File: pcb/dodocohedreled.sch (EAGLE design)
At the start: 11 parts

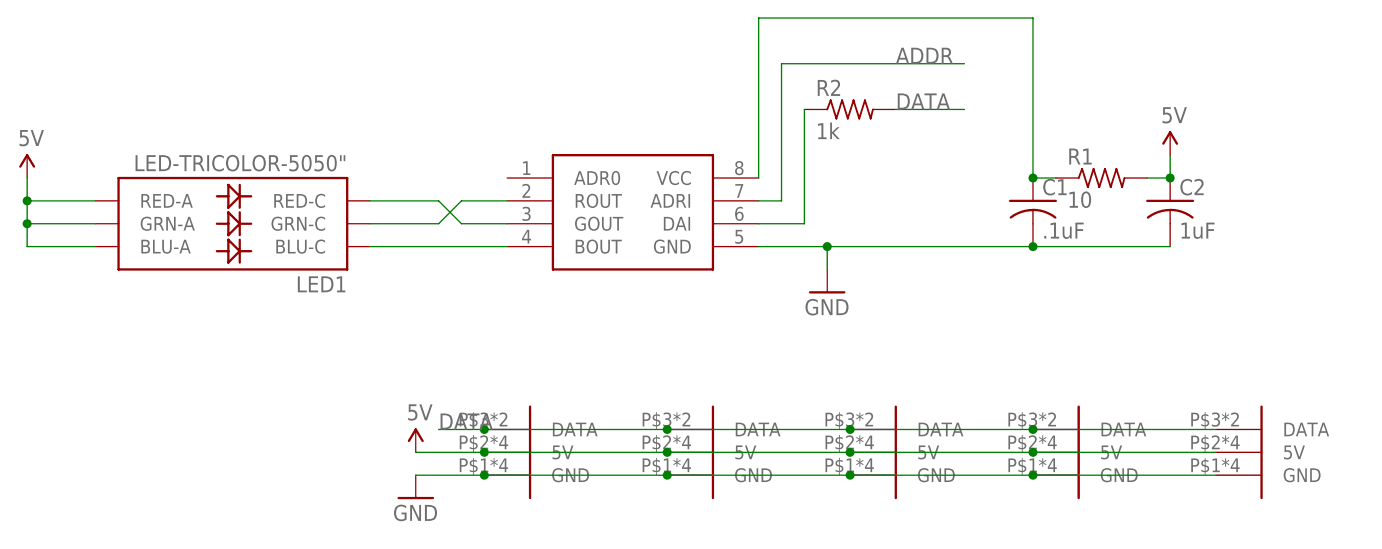
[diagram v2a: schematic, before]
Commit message: Switch to WS2822S module, bump to RevD.
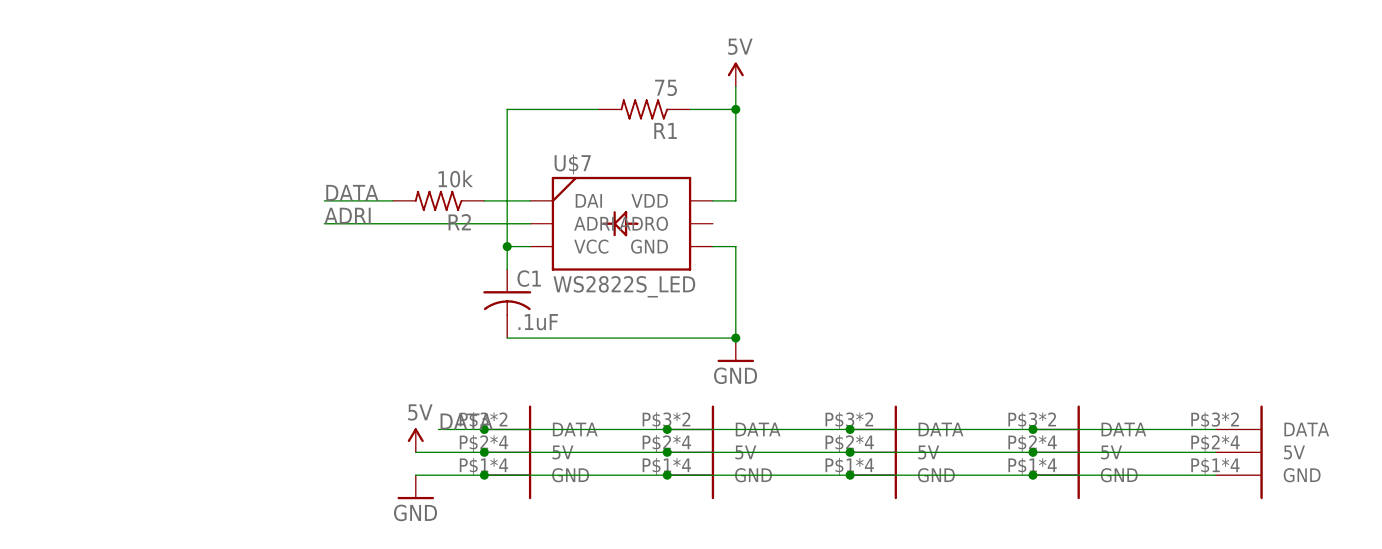
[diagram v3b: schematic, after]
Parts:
- removed C2: 1uF, adafruit:C-USC0603
- removed LED1: LED-TRICOLOR-5050", blinkinlabs:LED-TRICOLOR-5050"
- removed U$1: WS2821A, dodocohedreled:WS2821A
- added U$7: WS2822S_LED, blinkinlabs:WS2822S_LED
- R1: value 10 -> 75
- R2: value 1k -> 10k
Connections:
- removed net ADDR: U$1.ADRI
- removed net N$10: R2.1, U$1.DAI
- removed net N$3: LED1.RED-C, U$1.GOUT
- removed net N$6: C1.1, R1.1, U$1.VCC
- new net ADRI: U$7.ADRI
- net 5V: now also R1.1, U$7.VDD; no longer C2.1, LED1.BLU-A, LED1.GRN-A, LED1.RED-A, R1.2
- net GND: now also U$7.GND; no longer C2.2, U$1.GND
- net N$1: now also C1.1, R1.2, U$7.VCC; no longer LED1.GRN-C, U$1.ROUT
- net N$2: now also R2.1, U$7.DAI; no longer LED1.BLU-C, U$1.BOUT
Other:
- moved on the sheet: C1, R1, R2
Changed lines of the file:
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@@
 <?xml version="1.0" encoding="utf-8"?>
 <!DOCTYPE eagle SYSTEM "eagle.dtd">
-<eagle version="6.5.0">
+<eagle version="7.1.0">
 <drawing>
 <settings>
@@
 </classes>
 <parts>
-<part name="LED1" library="blinkinlabs" deviceset="LED-TRICOLOR-5050" device="&quot;"/>
-<part name="SUPPLY1" library="SparkFun-Aesthetics" deviceset="5V" device=""/>
 <part name="GND1" library="SparkFun-Aesthetics" deviceset="GND" device=""/>
-<part name="U$1" library="dodocohedreled" deviceset="WS2821A" device=""/>
 <part name="C1" library="adafruit" deviceset="C-US" device="C0603" value=".1uF"/>
-<part name="C2" library="adafruit" deviceset="C-US" device="C0603" value="1uF"/>
-<part name="R1" library="adafruit" deviceset="R-US_" device="R0603" value="10"/>
-<part name="R2" library="adafruit" deviceset="R-US_" device="R0603" value="1k"/>
+<part name="R1" library="adafruit" deviceset="R-US_" device="R0603" value="75"/>
+<part name="R2" library="adafruit" deviceset="R-US_" device="R0603" value="10k"/>
 <part name="SUPPLY2" library="SparkFun-Aesthetics" deviceset="5V" device=""/>
 <part name="U$2" library="dodocohedreled" deviceset="D_EDGE" device="SLOT"/>
@@
 <part name="U$5" library="dodocohedreled" deviceset="D_EDGE" device="SLOT"/>
 <part name="U$6" library="dodocohedreled" deviceset="D_EDGE" device="SLOT"/>
+<part name="U$7" library="blinkinlabs" deviceset="WS2822S_LED" device=""/>
 </parts>
 <sheets>
@@
 </plain>
 <instances>
-<instance part="LED1" gate="G$1" x="15.24" y="81.28" rot="R180"/>
-<instance part="SUPPLY1" gate="G$1" x="-7.62" y="86.36"/>
-<instance part="GND1" gate="1" x="81.28" y="73.66"/>
-<instance part="U$1" gate="G$1" x="53.34" y="81.28"/>
-<instance part="C1" gate="G$1" x="104.14" y="83.82"/>
-<instance part="C2" gate="G$1" x="119.38" y="83.82"/>
-<instance part="R1" gate="G$1" x="111.76" y="86.36"/>
-<instance part="R2" gate="G$1" x="83.82" y="93.98"/>
-<instance part="SUPPLY2" gate="G$1" x="119.38" y="88.9"/>
+<instance part="GND1" gate="1" x="71.12" y="66.04"/>
+<instance part="C1" gate="G$1" x="45.72" y="73.66"/>
+<instance part="R1" gate="G$1" x="60.96" y="93.98" rot="R180"/>
+<instance part="R2" gate="G$1" x="38.1" y="83.82" rot="R180"/>
+<instance part="SUPPLY2" gate="G$1" x="71.12" y="96.52"/>
 <instance part="U$2" gate="G$1" x="124.46" y="58.42"/>
 <instance part="SUPPLY3" gate="G$1" x="35.56" y="55.88"/>
@@
 <instance part="U$5" gate="G$1" x="83.82" y="58.42"/>
 <instance part="U$6" gate="G$1" x="104.14" y="58.42"/>
+<instance part="U$7" gate="G$1" x="58.42" y="81.28"/>
 </instances>
 <busses>
@@
 <nets>
 <net name="5V" class="0">
-<segment>
-<pinref part="SUPPLY1" gate="G$1" pin="5V"/>
-<wire x1="-7.62" y1="86.36" x2="-7.62" y2="83.82" width="0.1524" layer="91"/>
-<pinref part="LED1" gate="G$1" pin="BLU-A"/>
-<wire x1="0" y1="78.74" x2="-7.62" y2="78.74" width="0.1524" layer="91"/>
-<wire x1="-7.62" y1="78.74" x2="-7.62" y2="81.28" width="0.1524" layer="91"/>
-<pinref part="LED1" gate="G$1" pin="GRN-A"/>
-<wire x1="0" y1="81.28" x2="-7.62" y2="81.28" width="0.1524" layer="91"/>
-<wire x1="-7.62" y1="81.28" x2="-7.62" y2="83.82" width="0.1524" layer="91"/>
-<pinref part="LED1" gate="G$1" pin="RED-A"/>
-<wire x1="-7.62" y1="83.82" x2="0" y2="83.82" width="0.1524" layer="91"/>
-<junction x="-7.62" y="81.28"/>
-<junction x="-7.62" y="83.82"/>
-</segment>
-<segment>
-<pinref part="R1" gate="G$1" pin="2"/>
-<pinref part="C2" gate="G$1" pin="1"/>
-<wire x1="116.84" y1="86.36" x2="119.38" y2="86.36" width="0.1524" layer="91"/>
-<pinref part="SUPPLY2" gate="G$1" pin="5V"/>
-<wire x1="119.38" y1="88.9" x2="119.38" y2="86.36" width="0.1524" layer="91"/>
-<junction x="119.38" y="86.36"/>
-</segment>
 <segment>
 <pinref part="U$2" gate="G$1" pin="5V"/>
@@
 <junction x="104.14" y="55.88"/>
 </segment>
-</net>
-<net name="N$2" class="0">
-<segment>
-<pinref part="LED1" gate="G$1" pin="BLU-C"/>
-<pinref part="U$1" gate="G$1" pin="BOUT"/>
-<wire x1="30.48" y1="78.74" x2="45.72" y2="78.74" width="0.1524" layer="91"/>
+<segment>
+<pinref part="U$7" gate="G$1" pin="VDD"/>
+<wire x1="68.58" y1="83.82" x2="71.12" y2="83.82" width="0.1524" layer="91"/>
+<pinref part="SUPPLY2" gate="G$1" pin="5V"/>
+<wire x1="71.12" y1="83.82" x2="71.12" y2="93.98" width="0.1524" layer="91"/>
+<pinref part="R1" gate="G$1" pin="1"/>
+<wire x1="71.12" y1="93.98" x2="71.12" y2="96.52" width="0.1524" layer="91"/>
+<wire x1="66.04" y1="93.98" x2="71.12" y2="93.98" width="0.1524" layer="91"/>
+<junction x="71.12" y="93.98"/>
 </segment>
 </net>
 <net name="GND" class="0">
 <segment>
-<pinref part="U$1" gate="G$1" pin="GND"/>
-<wire x1="73.66" y1="78.74" x2="81.28" y2="78.74" width="0.1524" layer="91"/>
+<wire x1="71.12" y1="78.74" x2="71.12" y2="68.58" width="0.1524" layer="91"/>
 <pinref part="GND1" gate="1" pin="GND"/>
-<wire x1="81.28" y1="78.74" x2="81.28" y2="76.2" width="0.1524" layer="91"/>
-<pinref part="C2" gate="G$1" pin="2"/>
 <pinref part="C1" gate="G$1" pin="2"/>
-<wire x1="119.38" y1="78.74" x2="104.14" y2="78.74" width="0.1524" layer="91"/>
-<wire x1="104.14" y1="78.74" x2="81.28" y2="78.74" width="0.1524" layer="91"/>
-<junction x="81.28" y="78.74"/>
-<junction x="104.14" y="78.74"/>
+<wire x1="45.72" y1="68.58" x2="71.12" y2="68.58" width="0.1524" layer="91"/>
+<junction x="71.12" y="68.58"/>
+<pinref part="U$7" gate="G$1" pin="GND"/>
+<wire x1="71.12" y1="78.74" x2="68.58" y2="78.74" width="0.1524" layer="91"/>
 </segment>
 <segment>
@@
 </segment>
 </net>
-<net name="N$6" class="0">
-<segment>
-<pinref part="U$1" gate="G$1" pin="VCC"/>
-<pinref part="C1" gate="G$1" pin="1"/>
-<wire x1="73.66" y1="86.36" x2="73.66" y2="104.14" width="0.1524" layer="91"/>
-<wire x1="73.66" y1="104.14" x2="104.14" y2="104.14" width="0.1524" layer="91"/>
-<wire x1="104.14" y1="104.14" x2="104.14" y2="86.36" width="0.1524" layer="91"/>
-<pinref part="R1" gate="G$1" pin="1"/>
-<wire x1="104.14" y1="86.36" x2="106.68" y2="86.36" width="0.1524" layer="91"/>
-<junction x="104.14" y="86.36"/>
-</segment>
-</net>
-<net name="ADDR" class="0">
-<segment>
-<wire x1="76.2" y1="99.06" x2="76.2" y2="83.82" width="0.1524" layer="91"/>
-<pinref part="U$1" gate="G$1" pin="ADRI"/>
-<wire x1="76.2" y1="83.82" x2="73.66" y2="83.82" width="0.1524" layer="91"/>
-<wire x1="76.2" y1="99.06" x2="96.52" y2="99.06" width="0.1524" layer="91"/>
-<label x="88.9" y="99.06" size="1.778" layer="95"/>
-</segment>
-</net>
-<net name="N$10" class="0">
-<segment>
-<pinref part="U$1" gate="G$1" pin="DAI"/>
-<pinref part="R2" gate="G$1" pin="1"/>
-<wire x1="73.66" y1="81.28" x2="78.74" y2="81.28" width="0.1524" layer="91"/>
-<wire x1="78.74" y1="81.28" x2="78.74" y2="93.98" width="0.1524" layer="91"/>
+<net name="ADRI" class="0">
+<segment>
+<wire x1="48.26" y1="81.28" x2="25.4" y2="81.28" width="0.1524" layer="91"/>
+<label x="25.4" y="81.28" size="1.778" layer="95"/>
+<pinref part="U$7" gate="G$1" pin="ADRI"/>
 </segment>
 </net>
@@
 <segment>
 <pinref part="R2" gate="G$1" pin="2"/>
-<wire x1="88.9" y1="93.98" x2="96.52" y2="93.98" width="0.1524" layer="91"/>
-<label x="88.9" y="93.98" size="1.778" layer="95"/>
+<wire x1="33.02" y1="83.82" x2="25.4" y2="83.82" width="0.1524" layer="91"/>
+<label x="25.4" y="83.82" size="1.778" layer="95"/>
 </segment>
 <segment>
@@
 <net name="N$1" class="0">
 <segment>
-<pinref part="U$1" gate="G$1" pin="ROUT"/>
-<wire x1="45.72" y1="83.82" x2="40.64" y2="83.82" width="0.1524" layer="91"/>
-<wire x1="40.64" y1="83.82" x2="38.1" y2="81.28" width="0.1524" layer="91"/>
-<pinref part="LED1" gate="G$1" pin="GRN-C"/>
-<wire x1="38.1" y1="81.28" x2="30.48" y2="81.28" width="0.1524" layer="91"/>
-</segment>
-</net>
-<net name="N$3" class="0">
-<segment>
-<pinref part="LED1" gate="G$1" pin="RED-C"/>
-<wire x1="30.48" y1="83.82" x2="38.1" y2="83.82" width="0.1524" layer="91"/>
-<wire x1="38.1" y1="83.82" x2="40.64" y2="81.28" width="0.1524" layer="91"/>
-<pinref part="U$1" gate="G$1" pin="GOUT"/>
-<wire x1="40.64" y1="81.28" x2="45.72" y2="81.28" width="0.1524" layer="91"/>
-</segment>
-</net>
+<pinref part="U$7" gate="G$1" pin="VCC"/>
+<pinref part="C1" gate="G$1" pin="1"/>
+<wire x1="48.26" y1="78.74" x2="45.72" y2="78.74" width="0.1524" layer="91"/>
+<wire x1="45.72" y1="78.74" x2="45.72" y2="76.2" width="0.1524" layer="91"/>
+<wire x1="45.72" y1="78.74" x2="45.72" y2="93.98" width="0.1524" layer="91"/>
+<pinref part="R1" gate="G$1" pin="2"/>
+<wire x1="45.72" y1="93.98" x2="55.88" y2="93.98" width="0.1524" layer="91"/>
+<junction x="45.72" y="78.74"/>
+</segment>
+</net>
+<net name="N$2" class="0">
+<segment>
+<pinref part="U$7" gate="G$1" pin="DAI"/>
+<pinref part="R2" gate="G$1" pin="1"/>
+<wire x1="48.26" y1="83.82" x2="43.18" y2="83.82" width="0.1524" layer="91"/>
+</segment>
+</net>
